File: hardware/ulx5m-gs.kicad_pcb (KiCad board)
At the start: 6 copper layers, 55 x 40 mm, 301 parts, among them J1 DF40C-100DP-0.4V_51_, J2 DF40C-100DP-0.4V_51_, J3 Vcore_sel, J4 JTAG, J5 USB_C_Receptacle, Q1 BSS138, Q2 BSS138, SW1 219-2MST, U1 TLV75718PDBV, U10 IS42S16320D-6BLI, U14 KSZ9031RNXCA, U2 TLV75733PDBV, U3 MPM3833CGRH-Z, U4 GateMate-CCGM1A1, U5 TLV75712PDBV, U6 74LVC1G04GM,115, U7 74LVC2G00HK3-7, U8 74LVC2G00HK3-7, U9 AT25QL321-MBUE-T, X1 ECS-2520MV-250-xx, X2 511FCA100M000BAG, Y1 ASE2-25.000MHZ-L-C-T

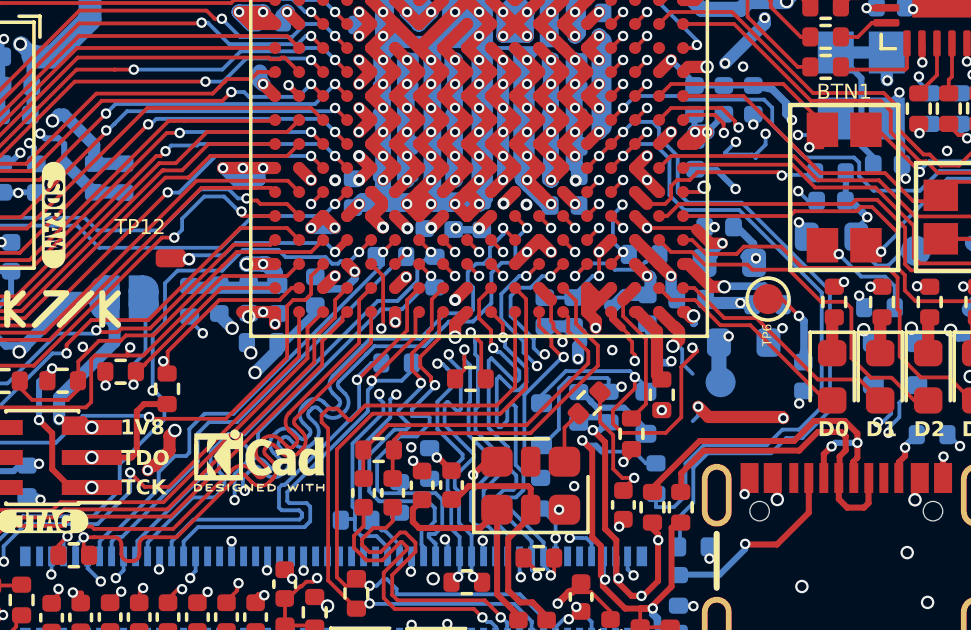
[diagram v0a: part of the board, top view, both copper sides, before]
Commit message: power: removed rc filters from gpio domains
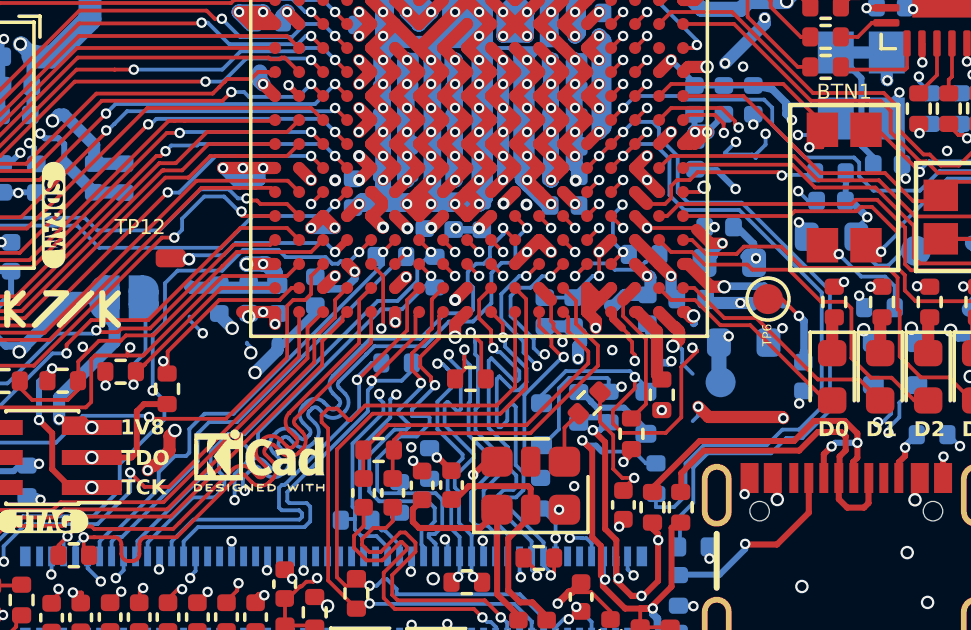
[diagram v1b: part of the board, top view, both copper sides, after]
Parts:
- removed R121, R122, R123: 4R7, Resistor_SMD:R_0402_1005Metric
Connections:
- C43 pad 1: /config/+1V8_FLASH -> VDD_CLK
- C44 pad 1: /config/+1V8_FLASH -> VDD_CLK
- C45 pad 1: /config/+1V8_FLASH -> VDD_CLK
- C50 pad 1: /lvds/+1V2_SA -> +1V2
- C51 pad 1: /lvds/+1V2_SA -> +1V2
- C52 pad 1: /lvds/+1V2_SA -> +1V2
- C53 pad 1: /lvds/+1V8_SB -> VDD_CLK
- C54 pad 1: /lvds/+1V8_SB -> VDD_CLK
- C55 pad 1: /lvds/+1V8_SB -> VDD_CLK
- U4 pad N11: /lvds/+1V8_SB -> VDD_CLK
- U4 pad N13: /lvds/+1V8_SB -> VDD_CLK
- U4 pad N18: /lvds/+1V8_SB -> VDD_CLK
- U4 pad N5: /config/+1V8_FLASH -> VDD_CLK
- U4 pad P10: /lvds/+1V2_SA -> +1V2
- U4 pad P3: /config/+1V8_FLASH -> VDD_CLK
- U4 pad P5: /config/+1V8_FLASH -> VDD_CLK
- U4 pad P6: /lvds/+1V2_SA -> +1V2
- U4 pad P8: /lvds/+1V2_SA -> +1V2
- U4 pad R15: /lvds/+1V8_SB -> VDD_CLK
- U4 pad T1: /config/+1V8_FLASH -> VDD_CLK
- U4 pad T18: /lvds/+1V8_SB -> VDD_CLK
- U4 pad U3: /config/+1V8_FLASH -> VDD_CLK
- U4 pad U6: /lvds/+1V2_SA -> +1V2
- U4 pad U9: /lvds/+1V2_SA -> +1V2
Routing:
- net VDD_CLK: track 408.2 -> 471.9 mm, vias 52 -> 64
- net /lvds/+1V8_SB: track 41.0 -> 0.00 mm, vias 6 -> 0
- net /lvds/+1V2_SA: track 40.1 -> 0.00 mm, vias 7 -> 0
- net +1V2: track 100.6 -> 140.7 mm, vias 13 -> 20
- net /config/+1V8_FLASH: track 22.7 -> 0.00 mm, vias 6 -> 0
- removed copper zone on In3.Cu, net /config/+1V8_FLASH
- removed copper zone on In3.Cu, net /lvds/+1V2_SA
- removed copper zone on In3.Cu, net /lvds/+1V8_SB

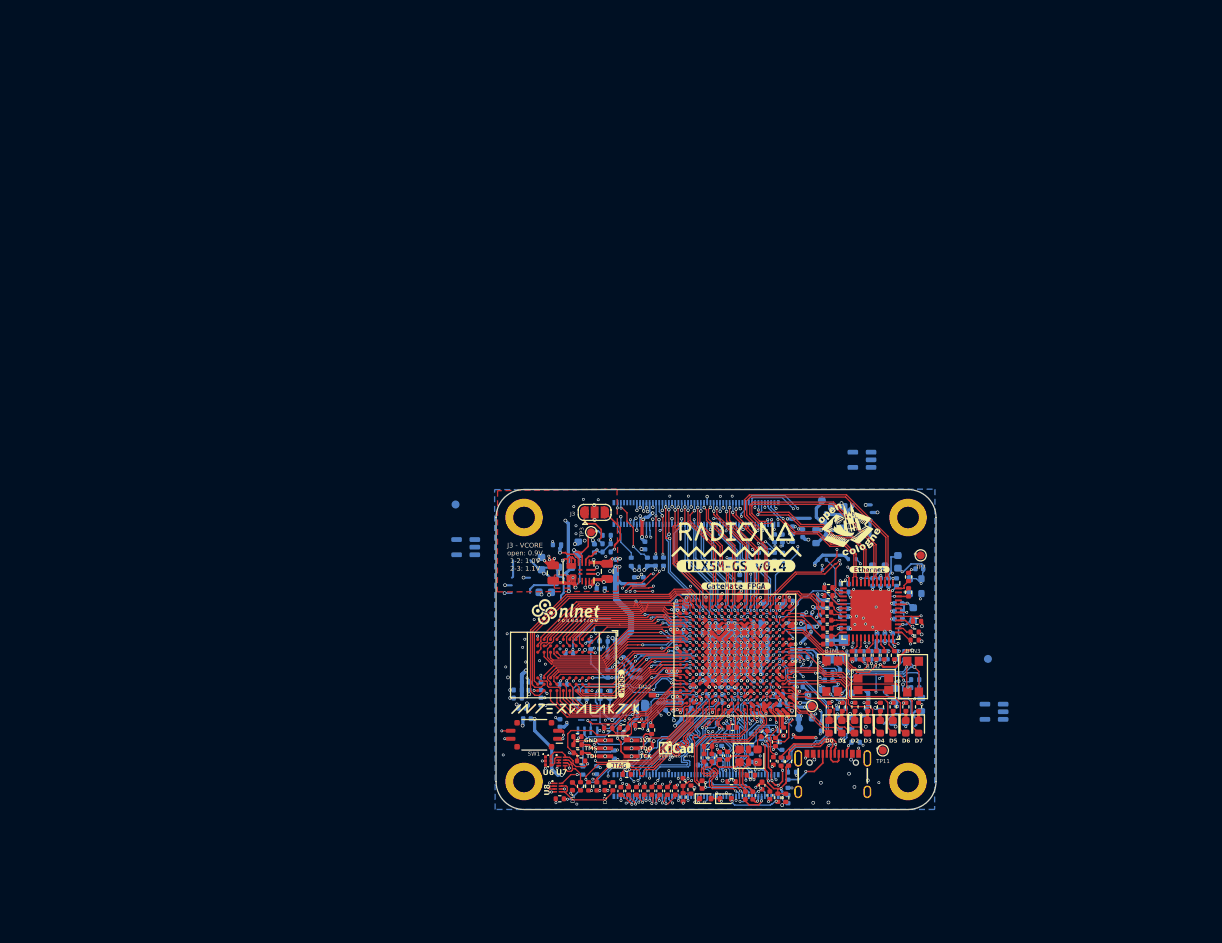
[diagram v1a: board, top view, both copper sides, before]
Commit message: big oopsie: change to 4 layer pcb, needs full revision
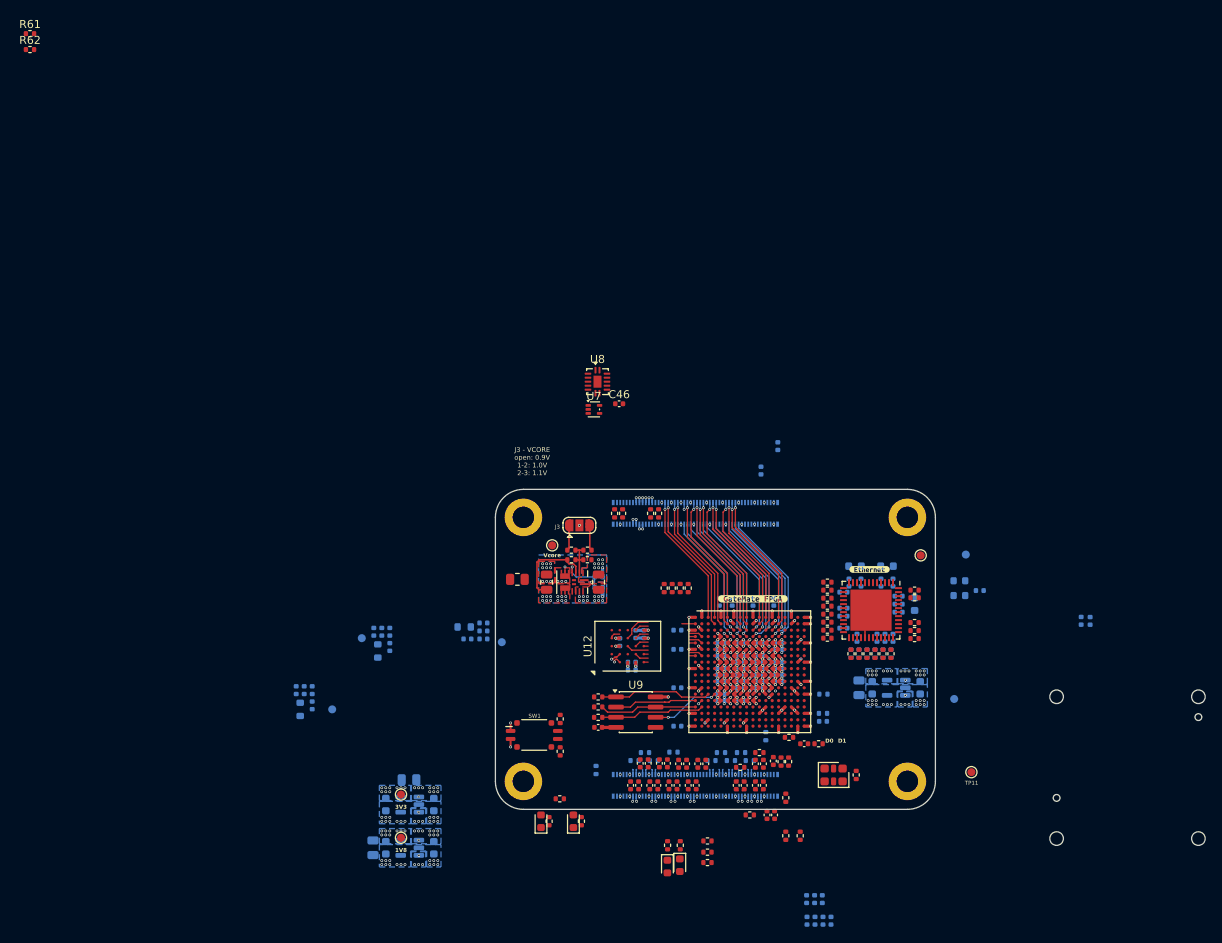
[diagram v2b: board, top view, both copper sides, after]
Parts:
- removed BTN1, BTN2, BTN3: SW_Push, Switch_EVPAA:Switch_EVPAA
- removed C101, C140, C141, C99: 22nF, Capacitor_SMD:C_0402_1005Metric
- removed C14, C17, C22, C27: 100n, Capacitor_SMD:C_0402_1005Metric
- removed C32, C35, C38, C4, C41: 10n, Capacitor_SMD:C_0402_1005Metric
- removed C85: 2.2uF, Capacitor_SMD:C_0402_1005Metric
- removed D11, D12, D13, D14, D15, D16: LED, LED_SMD:LED_0603_1608Metric
- removed D3, D4: 3.6V, Diode_SMD:D_SOD-523
- removed D5, D6, D7, D8: 1N914, Diode_SMD:D_SOD-523
- removed G***: LOGO, nlnet:nlnet
- removed G***: LOGO, kicad:kicad2_5mm
- removed G***: LOGO, intergalaktik:intergalaktik
- removed J4: JTAG, Connector_PinHeader_1.00mm:PinHeader_2x03_P1.00mm_Vertical_SMD
- removed J5: USB_C_Receptacle, ulx5m-gs:USB-C_16
- removed JP1: POR_EN, Jumper:SolderJumper-2_P1.3mm_Open_RoundedPad1.0x1.5mm
- removed LoGo_opencologne: MountingHole, OpenCologne:open_cologne_small
- removed Q1, Q2: BSS138, Package_TO_SOT_SMD:SOT-523
- removed R115: dnp, Resistor_SMD:R_0402_1005Metric
- removed R116, R141, R142: 0R, Resistor_SMD:R_0402_1005Metric
- removed R118, R64, R65, R86, R87, R88, R95: R300, Resistor_SMD:R_0402_1005Metric
- removed R136: 150R, Resistor_SMD:R_0402_1005Metric
- removed R144, R145, R146: 1K, Resistor_SMD:R_0402_1005Metric
- removed R37, R40, R41, R42, R43: 27R, Resistor_SMD:R_0402_1005Metric
- removed R46, R48: 1k, Resistor_SMD:R_0402_1005Metric
- removed R47, R55: 12k1, Resistor_SMD:R_0402_1005Metric
- removed TP12: SPI_FWD, TestPoint:TestPoint_Pad_1.0x1.0mm
- removed U10: IS42S16320D-6BLI, IS42S16320D:IS42S16320D-6BLI
- removed U6: 74LVC1G04GM,115, 74LVC1G04GM,115:PESD3V3L5UF115
- removed Y1: ASE2-25.000MHZ-L-C-T, Crystal:Crystal_SMD_TXC_7M-4Pin_3.2x2.5mm
- removed kibuzzard-686AA726: G***, kibuzzard-686AA726
- removed kibuzzard-686AA7AF: G***, kibuzzard-686AA7AF
- removed kibuzzard-68DC261C: G***, kibuzzard-68DC261C
- removed radiona: radiona, radiona:radiona
- added C12: 220n, Capacitor_SMD:C_0402_1005Metric, F.Cu at (83.2, 94.5)
- added C139: 10n, Capacitor_SMD:C_0402_1005Metric, B.Cu at (74.7, 76.6)
- added C19: 220n, Capacitor_SMD:C_0402_1005Metric, F.Cu at (85.4, 91.8)
- added C20: 220n, Capacitor_SMD:C_0402_1005Metric, F.Cu at (84.4, 91.8)
- added C24: 220n, Capacitor_SMD:C_0402_1005Metric, F.Cu at (81.8, 94.5)
- added C25: 220n, Capacitor_SMD:C_0402_1005Metric, F.Cu at (80.8, 94.5)
- added C46: 100n, Capacitor_SMD:C_0402_1005Metric, F.Cu at (74.6, 46.8)
- added C5: 220n, Capacitor_SMD:C_0402_1005Metric, F.Cu at (83.0, 91.8)
- added C6: 220n, Capacitor_SMD:C_0402_1005Metric, F.Cu at (82.0, 91.8)
- added C7: 220n, Capacitor_SMD:C_0402_1005Metric, F.Cu at (84.2, 94.5)
- added C81: 10n, Capacitor_SMD:C_0402_1005Metric, B.Cu at (76.7, 75.6)
- added C82: 10n, Capacitor_SMD:C_0402_1005Metric, B.Cu at (77.7, 75.6)
- added C83: 100n, Capacitor_SMD:C_0402_1005Metric, B.Cu at (76.2, 80.1)
- added C84: 100n, Capacitor_SMD:C_0402_1005Metric, B.Cu at (76.2, 79.1)
- added U12: S27KL0641, Package_BGA:BGA-24_6x8mm_Layout5x5_P1.0mm, F.Cu at (75.7, 77.1)
- C48, R108, R12, R128, R134, R138, R139, R14, R147, R148, R149, R15, R150, R16, R33, R35, R38, R61, R62, TP1, TP2: moved to F.Cu
- D1, D2: footprint Diode_SMD:D_0402_1005Metric -> Diode_SMD:D_0603_1608Metric
- R10, R11, R21: footprint Resistor_SMD:R_0603_1608Metric -> Resistor_SMD:R_0805_2012Metric
- R129, R130, R131, R132, R135: value 150R -> 150
- R13: footprint Resistor_SMD:R_0603_1608Metric -> Resistor_SMD:R_0805_2012Metric; moved to F.Cu
- R30, TP6: moved to B.Cu
- R50, R51, R54: value 150R -> 150; moved to B.Cu
- R58: value 1k -> 1k5
- U7: value 74LVC2G00HK3-7 -> 74LVC1GU04DRL; footprint 74LVC2G00HK3-7:74LVC2G00HK37 -> Package_TO_SOT_SMD:SOT-553
- U8: value 74LVC2G00HK3-7 -> SN74AUC00; footprint 74LVC2G00HK3-7:74LVC2G00HK37 -> Package_DFN_QFN:DHVQFN-14-1EP_2.5x3mm_P0.5mm_EP1x1.5mm
- U9: footprint ulx5m-gs:SON80P400X300X60-10N -> Package_SO:SOIC-8_3.9x4.9mm_P1.27mm; moved to F.Cu
- moved R62 134.7 mm to (0.95, 2.48), turned to 0 degrees
- moved R61 133.3 mm to (0.95, 0.49), turned to 0 degrees
- moved U1 74.5 mm to (48.4, 102.3)
- moved C8 69.1 mm to (45.4, 102.3)
- moved R10 67.7 mm to (43.8, 102.3), turned to -90 degrees
- moved TP1 67.4 mm to (47.3, 101.0), turned to 0 degrees
- moved C2 66.1 mm to (51.4, 102.3), turned to -90 degrees
- moved C42 63.7 mm to (36.2, 84.5), turned to 90 degrees
- moved R23 62.7 mm to (34.7, 85.0), turned to 90 degrees
- moved C36 61.8 mm to (35.2, 82.6), turned to -90 degrees
- moved TP6 60.0 mm to (38.7, 85.0), turned to 0 degrees
- moved C33 57.2 mm to (34.2, 82.6)
- moved C122 55.8 mm to (43.9, 75.3)
- moved TP8 55.8 mm to (42.4, 76.1)
- moved R105 54.1 mm to (44.4, 77.7), turned to 90 degrees
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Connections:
- net Net-(R7-Pad1) renamed /power/TESTMODE
- net Net-(U1-OUT) renamed /power/DC_1V8
- net Net-(U2-OUT) renamed /power/DC_3V3
- net Net-(U3-OUT_S) renamed /power/DC_OUT
- net Net-(U3-SW-Pad15) renamed /power/SW
- net Net-(U5-OUT) renamed /power/DC_1V2
- C100 pad 1: VDD_CLK -> +1V8
- C102 pad 1: VDD_CLK -> +1V8
- C103 pad 1: VDD_CLK -> +1V8
- C105 pad 1: VDD_CLK -> +1V8
- C107 pad 1: VDD_CLK -> +1V8
- C110 pad 1: VDD_CLK -> +1V8
- C126 pad 1: VDD_CLK -> +1V8
- C131 pad 1: VDD_CLK -> +1V8
- C132 pad 1: VDD_CLK -> +1V8
- C43 pad 1: VDD_CLK -> +1V8
- C44 pad 1: VDD_CLK -> +1V8
- C45 pad 1: VDD_CLK -> +1V8
- C47 pad 1: VDD_CLK -> +1V8
- C48 pad 1: VDD_CLK -> +1V8
- C53 pad 1: VDD_CLK -> +1V8
- C54 pad 1: VDD_CLK -> +1V8
- C55 pad 1: VDD_CLK -> +1V8
- C56 pad 1: VDD_CLK -> +1V8
- C57 pad 1: SDRAM_VCC -> +1V8
- C58 pad 1: SDRAM_VCC -> +1V8
- C59 pad 1: /cm4-hsio/DDMI0_TX0_P -> /lvds/DDMI0_HS_TX0_P
- C59 pad 2: /lvds/DDMI0_HS_TX0_P -> /cm4-hsio/DDMI0_TX0_P
- C60 pad 1: /cm4-hsio/DDMI0_TX0_N -> /lvds/DDMI0_HS_TX0_N
- C60 pad 2: /lvds/DDMI0_HS_TX0_N -> /cm4-hsio/DDMI0_TX0_N
- C61 pad 1: /cm4-hsio/DDMI0_TX1_P -> /lvds/DDMI0_HS_TX1_P
- C61 pad 2: /lvds/DDMI0_HS_TX1_P -> /cm4-hsio/DDMI0_TX1_P
- C62 pad 1: /cm4-hsio/DDMI0_TX1_N -> /lvds/DDMI0_HS_TX1_N
- C62 pad 2: /lvds/DDMI0_HS_TX1_N -> /cm4-hsio/DDMI0_TX1_N
- C63 pad 1: /cm4-hsio/DDMI0_TX2_P -> /lvds/DDMI0_HS_TX2_P
- C63 pad 2: /lvds/DDMI0_HS_TX2_P -> /cm4-hsio/DDMI0_TX2_P
- C64 pad 1: /cm4-hsio/DDMI0_TX2_N -> /lvds/DDMI0_HS_TX2_N
- C64 pad 2: /lvds/DDMI0_HS_TX2_N -> /cm4-hsio/DDMI0_TX2_N
- C65 pad 1: /cm4-hsio/DDMI0_CLK_P -> /lvds/DDMI0_HS_CLK_P
- C65 pad 2: /lvds/DDMI0_HS_CLK_P -> /cm4-hsio/DDMI0_CLK_P
- C66 pad 1: /cm4-hsio/DDMI0_CLK_N -> /lvds/DDMI0_HS_CLK_N
- C66 pad 2: /lvds/DDMI0_HS_CLK_N -> /cm4-hsio/DDMI0_CLK_N
- C75 pad 1: SDRAM_VCC -> +1V8
- C76 pad 1: SDRAM_VCC -> +1V8
- C77 pad 1: SDRAM_VCC -> +1V8
- C78 pad 1: SDRAM_VCC -> +1V8
- C79 pad 1: SDRAM_VCC -> +1V8
- C80 pad 1: SDRAM_VCC -> +1V8
- C86 pad 1: SDRAM_VCC -> GPIO_VREF
- C87 pad 1: SDRAM_VCC -> GPIO_VREF
- C88 pad 1: SDRAM_VCC -> GPIO_VREF
- C89 pad 1: SDRAM_VCC -> GPIO_VREF
- C90 pad 1: SDRAM_VCC -> GPIO_VREF
- C91 pad 1: SDRAM_VCC -> GPIO_VREF
- C92 pad 1: SDRAM_VCC -> GPIO_VREF
- C93 pad 1: SDRAM_VCC -> GPIO_VREF
- C98 pad 1: VDD_CLK -> +1V8
- J1 pad 28: /cm4-hsio/USB3_0_D0_N -> unconnected-(J1-Pad28)
- J1 pad 30: /cm4-hsio/USB3_0_D0_P -> unconnected-(J1-Pad30)
- J1 pad 34: /cm4-hsio/USB3_0_D1_N -> unconnected-(J1-Pad34)
- J1 pad 36: /cm4-hsio/USB3_0_D1_P -> unconnected-(J1-Pad36)
- J1 pad 40: /cm4-hsio/USB3_0_C_N -> unconnected-(J1-Pad40)
- J1 pad 42: /cm4-hsio/USB3_0_C_P -> unconnected-(J1-Pad42)
- J2 pad 19: /cm4-gpio/FAN_PWM -> unconnected-(J2-Pad19)
- J2 pad 35: /cm4-gpio/ID_SC -> unconnected-(J2-Pad35)
- J2 pad 36: /cm4-gpio/ID_SD -> unconnected-(J2-Pad36)
- J2 pad 78: /cm4-gpio/GPIO_VREF -> GPIO_VREF
- J2 pad 88: VDD_CLK -> +1V8
- J2 pad 90: VDD_CLK -> +1V8
- J2 pad 94: unconnected-(J2-Pad94) -> Net-(J2-Pad94)
- J2 pad 96: unconnected-(J2-Pad96) -> Net-(J2-Pad96)
- R10 pad 2: VDD_CLK -> +1V8
- R111 pad 1: VDD_CLK -> +1V8
- R112 pad 1: VDD_CLK -> +1V8
- R143 pad 1: VDD_CLK -> +1V8
- R30 pad 1: /config/JTAG_POR -> +1V8
- R31 pad 1: Net-(U7-1Y) -> Net-(R31-Pad1)
- R32 pad 1: Net-(U8-1Y) -> Net-(R32-Pad1)
- R33 pad 1: VDD_CLK -> +1V8
- R34 pad 1: VDD_CLK -> +1V8
- R35 pad 1: VDD_CLK -> +1V8
- R36 pad 1: VDD_CLK -> +1V8
- R38 pad 1: VDD_CLK -> +1V8
- R44 pad 1: /cm4-hsio/USB_N -> Net-(U4D-IO_EA_B0)
- R44 pad 2: /ethernet/FPD1- -> /cm4-hsio/USB_N
- R45 pad 1: /cm4-hsio/USB_P -> Net-(U4D-IO_EA_A0)
- R45 pad 2: /ethernet/FPD1+ -> /cm4-hsio/USB_P
- R61 pad 2: /cm4-gpio/USB_CC1 -> Net-(J2-Pad94)
- R62 pad 2: /cm4-gpio/USB_CC2 -> Net-(J2-Pad96)
- R66 pad 1: VDD_CLK -> +1V8
- R67 pad 1: VDD_CLK -> +1V8
- R70 pad 1: VDD_CLK -> +1V8
- R71 pad 1: VDD_CLK -> +1V8
- R72 pad 1: VDD_CLK -> +1V8
- R73 pad 1: VDD_CLK -> +1V8
- R96 pad 1: VDD_CLK -> +1V8
- SW1 pad 1: VDD_CLK -> +1V8
- SW1 pad 2: VDD_CLK -> +1V8
- U1 pad 4: unconnected-(U1-NC-Pad4) -> GND
- U14 pad 15: /ethernet/LEDY -> /cm4-gpio/ETH0_LEDY
- U14 pad 16: VDD_CLK -> +1V8
- U14 pad 17: /ethernet/LEDG -> /cm4-gpio/ETH0_LEDG
- U14 pad 34: VDD_CLK -> +1V8
- U14 pad 40: VDD_CLK -> +1V8
- U2 pad 4: unconnected-(U2-NC-Pad4) -> GND
- U4 pad A16: VDD_CLK -> +1V8
- U4 pad A2: SDRAM_VCC -> +1V8
- U4 pad A3: SDRAM_A1 -> /cm4-gpio/SD_DAT2
- U4 pad A5: SDRAM_VCC -> GPIO_VREF
- U4 pad A6: /cm4-gpio/GPIO14 -> /cm4-gpio/GPIO15
- U4 pad A8: /cm4-gpio/GPIO18 -> /cm4-gpio/GPIO23
- U4 pad A9: /cm4-gpio/GPIO24 -> /cm4-gpio/GPIO25
- U4 pad B1: SDRAM_A12 -> /memory/~{HR_RST}
- U4 pad B10: SDRAM_VCC -> GPIO_VREF
- U4 pad B13: SDRAM_VCC -> GPIO_VREF
- U4 pad B18: VDD_CLK -> +1V8
- U4 pad B2: SDRAM_A4 -> PWR_BTN
- U4 pad B3: SDRAM_A2 -> /cm4-gpio/SDA0
- U4 pad B4: SDRAM_A10 -> /cm4-gpio/SD_DAT1
- U4 pad B6: /cm4-gpio/GPIO15 -> /cm4-gpio/GPIO14
- U4 pad B7: SDRAM_VCC -> GPIO_VREF
- U4 pad B8: /cm4-gpio/GPIO23 -> /cm4-gpio/GPIO18
- U4 pad B9: /cm4-gpio/GPIO25 -> /cm4-gpio/GPIO24
- U4 pad C11: /cm4-gpio/GPIO11 -> /cm4-gpio/GPIO9
- U4 pad C14: /cm4-gpio/GPIO19 -> /cm4-gpio/GPIO13
- U4 pad C2: SDRAM_VCC -> +1V8
- U4 pad C3: SDRAM_A8 -> unconnected-(U4F-IO_WC_A7-PadC3)
- U4 pad C4: SDRAM_A5 -> unconnected-(U4F-IO_WC_B7-PadC4)
- U4 pad C5: /cm4-gpio/SD_DAT2 -> /cm4-gpio/SCL0
- U4 pad C8: /cm4-gpio/GPIO17 -> /cm4-gpio/GPIO4
- U4 pad D1: SDRAM_D10 -> /memory/HR_RWDS
- U4 pad D10: /cm4-gpio/GPIO9 -> /cm4-gpio/GPIO11
- U4 pad D11: /cm4-gpio/FAN_PWM -> unconnected-(U4C-IO_NB_A3-PadD11)
- U4 pad D12: /cm4-gpio/SD_DAT1 -> unconnected-(U4C-IO_NB_A5-PadD12)
- U4 pad D13: /cm4-gpio/GPIO13 -> /cm4-gpio/GPIO19
- U4 pad D2: SDRAM_DQM1 -> /memory/~{HR_CS}
- U4 pad D3: SDRAM_D8 -> unconnected-(U4F-IO_WC_A6-PadD3)
- U4 pad D4: SDRAM_A7 -> unconnected-(U4F-IO_WC_B6-PadD4)
- U4 pad D5: SDRAM_VCC -> +1V8
- U4 pad D8: /cm4-gpio/GPIO4 -> /cm4-gpio/GPIO17
- U4 pad E1: SDRAM_D15 -> /memory/HR_DQ6
- U4 pad E10: SDRAM_VCC -> GPIO_VREF
- U4 pad E12: SDRAM_VCC -> GPIO_VREF
- U4 pad E14: VDD_CLK -> +1V8
- U4 pad E17: VDD_CLK -> +1V8
- U4 pad E2: SDRAM_D12 -> /memory/HR_DQ0
- U4 pad E3: SDRAM_D11 -> /memory/HR_CK_P
- U4 pad E4: SDRAM_D9 -> /memory/HR_CK_N
- U4 pad E6: SDRAM_VCC -> GPIO_VREF
- U4 pad E8: SDRAM_VCC -> GPIO_VREF
- U4 pad F11: SDRAM_VCC -> GPIO_VREF
- U4 pad F13: VDD_CLK -> +1V8
- U4 pad F2: SDRAM_VCC -> +1V8
- U4 pad F3: SDRAM_D14 -> /memory/HR_DQ4
- U4 pad F4: SDRAM_D13 -> /memory/HR_DQ5
- U4 pad F5: SDRAM_VCC -> +1V8
- U4 pad F7: SDRAM_VCC -> GPIO_VREF
- U4 pad G1: SDRAM_A11 -> /memory/HR_DQ7
- U4 pad G18: PWR_BTN -> unconnected-(U4D-IO_EA_A7-PadG18)
- U4 pad G2: SDRAM_A9 -> /memory/HR_DQ1
- U4 pad G3: SDRAM_CLK -> /memory/HR_DQ2
- U4 pad G4: SDRAM_CKE -> /memory/HR_DQ3
- U4 pad H1: SDRAM_BA0 -> /memory/eMMC_DAT4
- U4 pad H15: /cm4-gpio/ID_SC -> unconnected-(U4D-IO_EA_B6-PadH15)
- U4 pad H16: /cm4-gpio/ID_SD -> unconnected-(U4D-IO_EA_A6-PadH16)
- U4 pad H2: SDRAM_A6 -> /memory/eMMC_DAT5
- U4 pad H3: SDRAM_BA1 -> /memory/eMMC_DAT6
- U4 pad H4: SDRAM_A0 -> /memory/eMMC_DAT7
- U4 pad H5: SDRAM_VCC -> +1V8
- U4 pad J15: /cm4-gpio/SCL0 -> unconnected-(U4D-IO_EA_B5-PadJ15)
- U4 pad J16: /cm4-gpio/SDA0 -> unconnected-(U4D-IO_EA_A5-PadJ16)
- U4 pad J17: /ethernet/BTN1 -> unconnected-(U4D-IO_EA_B4-PadJ17)
- U4 pad J18: /ethernet/BTN2 -> unconnected-(U4D-IO_EA_A4-PadJ18)
- U4 pad J2: SDRAM_VCC -> +1V8
- U4 pad J3: SDRAM_nRAS -> /memory/eMMC_DAT2
- U4 pad J4: SDRAM_nCAS -> /memory/eMMC_DAT3
- U4 pad K1: SDRAM_D4 -> /memory/eMMC_DAT0
- U4 pad K15: /ethernet/BTN3 -> unconnected-(U4D-IO_EA_B3-PadK15)
- U4 pad K17: /ethernet/USB_PULL_N -> unconnected-(U4D-IO_EA_B2-PadK17)
- U4 pad K18: /ethernet/USB_PULL_P -> unconnected-(U4D-IO_EA_A2-PadK18)
- U4 pad K2: SDRAM_D5 -> /memory/eMMC_DAT1
- U4 pad K3: SDRAM_D2 -> /memory/eMMC_STRB
- U4 pad K4: SDRAM_D0 -> /memory/eMMC_CMD
- U4 pad K5: SDRAM_VCC -> +1V8
- U4 pad L1: SDRAM_DQM0 -> unconnected-(U4F-IO_WB_A3-PadL1)
- U4 pad L15: /ethernet/USB25_N -> unconnected-(U4D-IO_EA_B1-PadL15)
- U4 pad L16: /ethernet/USB25_P -> unconnected-(U4D-IO_EA_A1-PadL16)
- U4 pad L2: SDRAM_D7 -> /memory/eMMC_CLK
- U4 pad L3: SDRAM_D3 -> unconnected-(U4F-IO_WB_A2-PadL3)
- U4 pad L4: SDRAM_D1 -> unconnected-(U4F-IO_WB_B2-PadL4)
- U4 pad M14: /ethernet/USB25_N -> Net-(U4D-IO_EA_B0)
- U4 pad M15: /ethernet/USB25_P -> Net-(U4D-IO_EA_A0)
- U4 pad M17: /lvds/LED7 -> /lvds/DDMI1_HS_CLK_P
- U4 pad M18: /lvds/LED6 -> /lvds/DDMI1_HS_CLK_N
- U4 pad M2: SDRAM_VCC -> +1V8
- U4 pad M3: SDRAM_A3 -> unconnected-(U4F-IO_WB_A1-PadM3)
- U4 pad M4: SDRAM_D6 -> unconnected-(U4F-IO_WB_B1-PadM4)
- U4 pad M5: SDRAM_VCC -> +1V8
- U4 pad N1: SDRAM_nCS -> unconnected-(U4F-IO_WB_A0-PadN1)
- U4 pad N11: VDD_CLK -> +1V8
- U4 pad N13: VDD_CLK -> +1V8
- U4 pad N14: /lvds/CLK_25MHz -> unconnected-(U4E-CLK0/IO_SB_A8-PadN14)
- U4 pad N15: RST_N -> unconnected-(U4E-IO_SB_B8-PadN15)
- U4 pad N18: VDD_CLK -> +1V8
- U4 pad N2: SDRAM_nWE -> unconnected-(U4F-IO_WB_B0-PadN2)
- U4 pad N5: VDD_CLK -> +1V8
- U4 pad P17: /lvds/LED5 -> /lvds/DDMI1_HS_TX2_P
- U4 pad P18: /lvds/LED4 -> /lvds/DDMI1_HS_TX2_N
- U4 pad P3: VDD_CLK -> +1V8
- U4 pad P5: VDD_CLK -> +1V8
- U4 pad R15: VDD_CLK -> +1V8
- U4 pad R17: /lvds/LED2 -> /lvds/DDMI1_HS_TX1_P
- U4 pad R18: /lvds/LED3 -> /lvds/DDMI1_HS_TX1_N
- U4 pad R4: Net-(U4B-IO_WA_B5/SPI_FWD) -> unconnected-(U4B-IO_WA_B5/SPI_FWD-PadR4)
- U4 pad T1: VDD_CLK -> +1V8
- U4 pad T14: VDD_CLK -> +1V8
- U4 pad T18: VDD_CLK -> +1V8
- U4 pad U1: /config/JTAG_POR -> +1V8
- U4 pad U17: /lvds/LED0 -> /lvds/DDMI1_HS_TX0_P
- U4 pad U18: /lvds/LED1 -> /lvds/DDMI1_HS_TX0_N
- U4 pad U3: VDD_CLK -> +1V8
- U4 pad U5: /cm4-hsio/LVDS1_D2_P -> /lvds/LED0
- U4 pad V5: /cm4-hsio/LVDS1_D2_N -> /lvds/LED1
- U5 pad 4: unconnected-(U5-NC-Pad4) -> GND
- U7 pad 1: Net-(U6-Y) -> unconnected-(U7-NC-Pad1)
- U7 pad 2: Net-(U7-1B) -> /config/CFG_DONE
- U7 pad 3: Net-(U7-1B) -> GND
- U7 pad 4: GND -> /cm4-gpio/nLED_act
- U7 pad 5: Net-(U7-1Y) -> +1V8
- U8 pad 2: Net-(U8-1B) -> Net-(U8-Pad2)
- U8 pad 3: Net-(U8-1B) -> Net-(R32-Pad1)
- U8 pad 4: GND -> Net-(R32-Pad1)
- U8 pad 5: Net-(U8-1Y) -> RST_N
- U8 pad 6: RST_N -> Net-(U8-Pad2)
- U8 pad 7: Net-(U8-1Y) -> GND
- U8 pad 8: VDD_CLK -> Net-(R31-Pad1)
- U9 pad 6: Net-(U9-SCLK) -> /config/SPI_SCK
- U9 pad 8: VDD_CLK -> +1V8
- X2 pad 6: VDD_CLK -> +1V8
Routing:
- net GND: track 1367.6 -> 695.0 mm, vias 298 -> 189
- net VDD_CLK: track 471.9 -> 0.00 mm, vias 64 -> 0
- net SDRAM_VCC: track 345.0 -> 0.00 mm, vias 45 -> 0
- net VDD_CORE: track 342.4 -> 28.3 mm, vias 40 -> 26
- net +3V3: track 271.2 -> 5.15 mm, vias 32 -> 9
- net +1V2: track 140.7 -> 4.53 mm, vias 20 -> 8
- net +5V: track 145.4 -> 10.4 mm, vias 21 -> 60
- net RST_N: track 105.7 -> 0.00 mm, vias 8 -> 0
- net /config/JTAG_TMS: track 72.6 -> 0.00 mm, vias 5 -> 0
- net /config/JTAG_TDI: track 61.9 -> 0.00 mm, vias 4 -> 0
- net /config/JTAG_TCK: track 58.9 -> 0.00 mm, vias 4 -> 0
- net /config/JTAG_TDO: track 46.0 -> 0.00 mm, vias 4 -> 0
- net PWR_BTN: track 42.2 -> 0.00 mm, vias 3 -> 0
- net /ethernet/RGMII_RX_DV: track 40.0 -> 0.00 mm, vias 2 -> 0
- net /ethernet/USB_PULL_P: track 39.5 -> 0.00 mm, vias 2 -> 0
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- added copper zone on In2.Cu, net +1V2
- added copper zone on In2.Cu, net +1V8
- added copper zone on In2.Cu, net +3V3
- added copper zone on B.Cu, net +5V
- added copper zone on F.Cu, net +5V
- added copper zone on In2.Cu, net +5V
- added copper zone on B.Cu, net /power/DC_1V2
- added copper zone on In2.Cu, net /power/DC_1V2
- added copper zone on B.Cu, net /power/DC_1V8
- added copper zone on In2.Cu, net /power/DC_1V8
- added copper zone on B.Cu, net /power/DC_3V3
- added copper zone on In2.Cu, net /power/DC_3V3
- added copper zone on In2.Cu, net /power/DC_OUT
- added copper zone on F.Cu, net /power/SW
- added copper zone on In2.Cu, net /power/SW
- added copper zone on In2.Cu, net GPIO_VREF
- added copper zone on In2.Cu, net VDD_CORE
- added copper zone on In2.Cu, net VDD_PLL
- added copper zone on In2.Cu, net VDD_SER
- added copper zone on In2.Cu, net VDD_SER_PLL
- removed copper zone on In3.Cu, net +1V2
- removed copper zone on In3.Cu, net +3V3
- removed copper zone on In3.Cu, net +5V
- removed copper zone on In2.Cu, net GND
- removed copper zone on In3.Cu, net GND
- removed copper zone on In4.Cu, net GND
- removed copper zone on In3.Cu, net SDRAM_VCC
- removed copper zone on In3.Cu, net VDD_CLK
- removed copper zone on In3.Cu, net VDD_CORE
- removed copper zone on In3.Cu, net VDD_SER
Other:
- board size 55 x 40 mm -> 88.7 x 44.5 mm
- copper layers 6 -> 4
- board text removed: "D2"
- board text removed: "D3"
- board text removed: "D4"
- board text removed: "D5"
- board text removed: "D6"
- board text removed: "D7"
- board text removed: "DDMI0 - 28mm PCIe - 25mm LVDS0 - 14mm LVDS1 - 17mm"
- board text removed: "GND"
- board text removed: "TCK"
- board text removed: "TDI"
- board text removed: "TDO"
- board text removed: "TMS"
